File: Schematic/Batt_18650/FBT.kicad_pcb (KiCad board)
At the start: 2 copper layers, 86.5 x 100.5 mm, 18 parts, among them J1 TRRS Connector 3.5, J2 Conn_01x04, SW1 SW_SPDT

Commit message: work on PCBs, logos, and case
did more work on 18650 battery model
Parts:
- removed BT+1: Battery cathode, Connector_PinHeader_2.54mm:PinHeader_1x01_P2.54mm_Vertical
- added ?: , , F.Cu at (92.8, 106.4)
- added BT-2: Battery anode, Connector_PinHeader_2.54mm:PinHeader_1x01_P2.54mm_Vertical, F.Cu at (92.8, 103.9)
- J2: value Conn_01x04 -> TRRS Connector 3.5; footprint Connector_JST:JST_PH_S4B-PH-K_1x04_P2.00mm_Horizontal -> My_Library:PJ-320A
- moved GY2 37.8 mm to (153.8, 143.8)
- moved IMU2 37.5 mm to (153.5, 138.6)
- moved J2 28.9 mm to (140.9, 110.9), turned to 0 degrees
- moved JP1 21.4 mm to (109.1, 68.8)
- moved JP2 12.6 mm to (106.1, 68.8), turned to -90 degrees
- turned IMU1 to -90 degrees
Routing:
- net ESP32_5V5: track 0.00 -> 77.6 mm, vias 0 -> 1
- net GND: track 0.00 -> 42.7 mm
- net Net-(CHGR1-5_VIN): track 0.00 -> 25.3 mm
- net ESP32_3V3: track 18.3 -> 0.00 mm
- net SCL_1: track 3.51 -> 15.3 mm
- net SDA_1: track 9.09 -> 19.5 mm
- net +BATT: track 0.00 -> 7.81 mm
- net Net-(D2-A): track 0.00 -> 7.67 mm
- net Net-(GY2-SCL): track 3.97 -> 0.00 mm
- net Net-(GY2-SDA): track 3.97 -> 0.00 mm
- removed copper zone on B.Cu, net GND
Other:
- board size 86.5 x 100.5 mm -> 86.5 x 77.9 mm

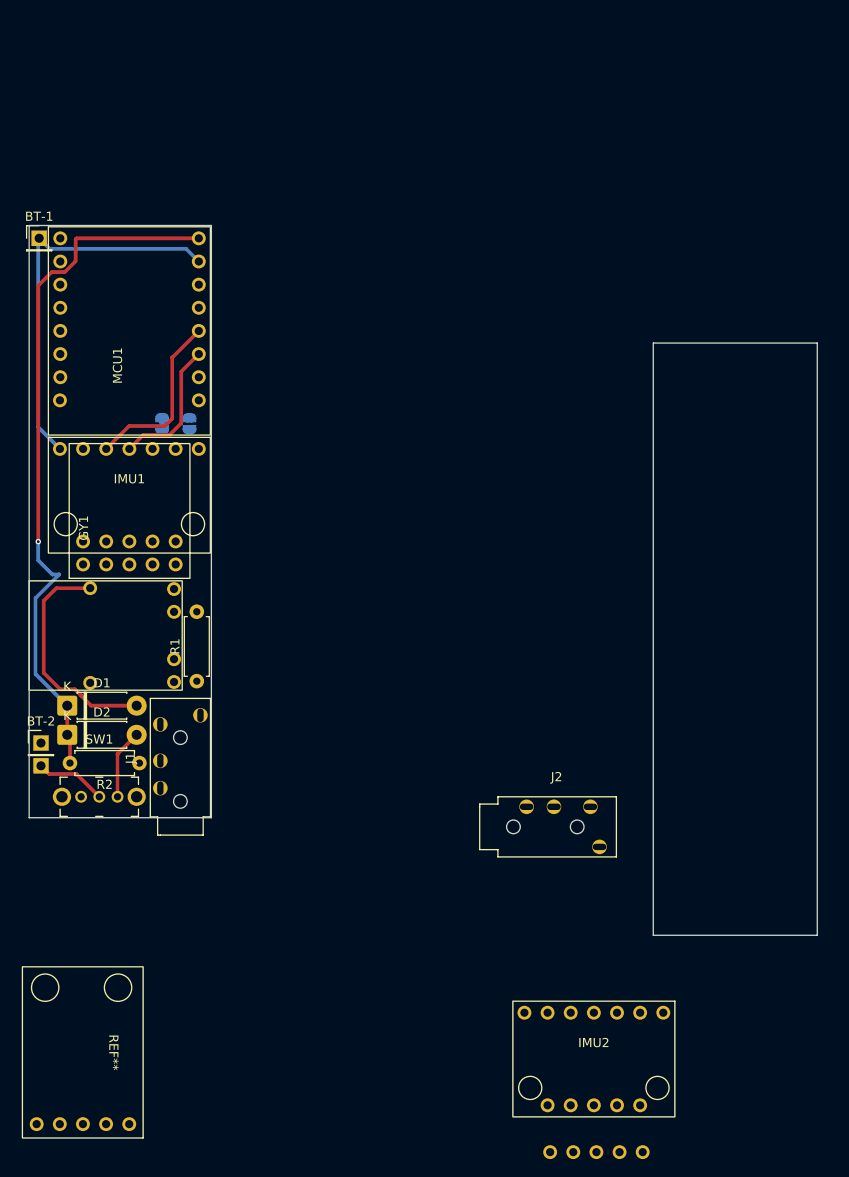
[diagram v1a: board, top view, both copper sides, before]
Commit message: Work on 18650 PCB
It's done, but I may re-do this one to flip the ESP32 sideways...
(I then proceeded to work on the sideways version)
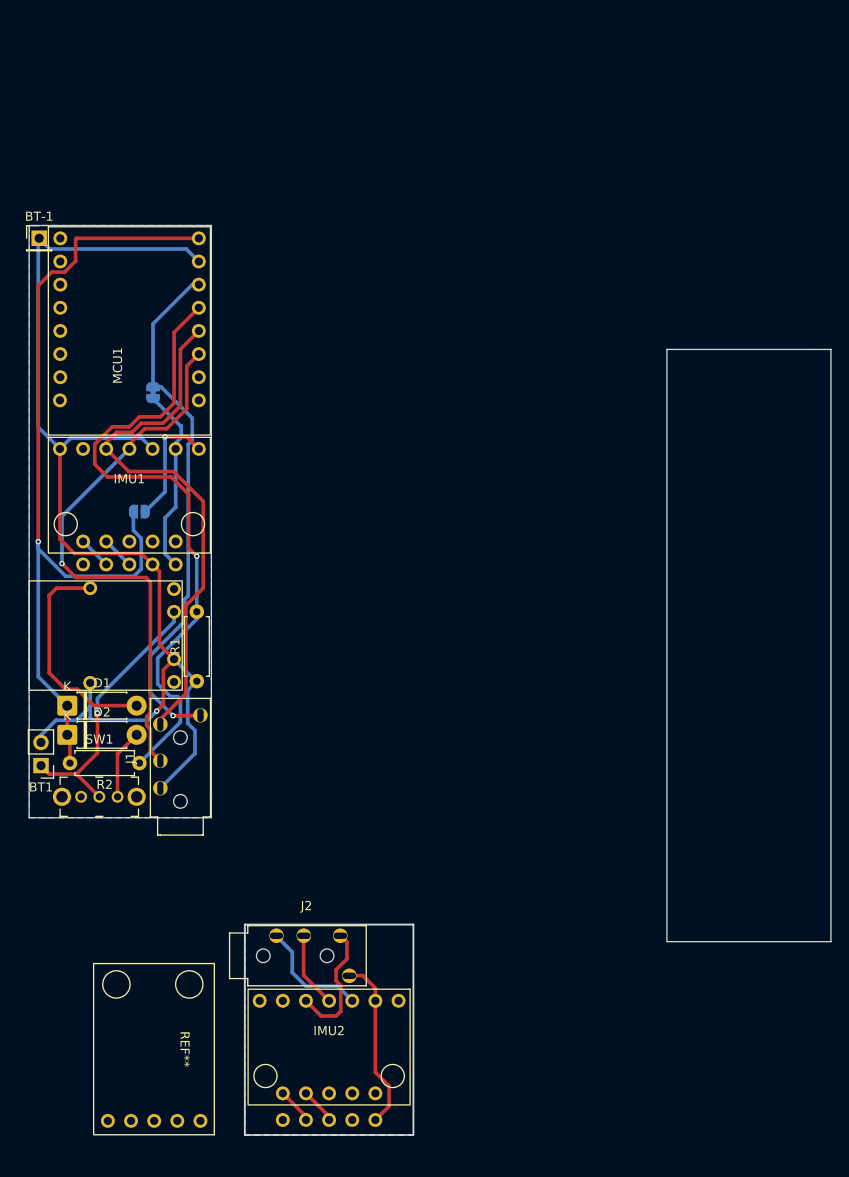
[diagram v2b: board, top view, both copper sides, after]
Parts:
- removed ?: , 
- removed BT-2: Battery anode, Connector_PinHeader_2.54mm:PinHeader_1x01_P2.54mm_Vertical
- added BT1: Battery, Connector_PinHeader_2.54mm:PinHeader_1x02_P2.54mm_Vertical, F.Cu at (92.8, 106.4)
- GY1: moved to B.Cu
- moved J2 30.9 mm to (113.5, 125.0)
- moved GY2 29.6 mm to (124.4, 140.3)
- moved IMU2 29.1 mm to (124.4, 137.3)
- moved JP1 11.1 mm to (103.6, 78.5), turned to 180 degrees
- moved REF** 7.82 mm to (105.1, 137.4)
- moved JP2 3.54 mm to (105.1, 65.5)
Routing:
- net GND: track 42.7 -> 142.3 mm, vias 0 -> 1
- net ESP32_3V3: track 0.00 -> 77.2 mm, vias 0 -> 1
- net BATTERY_READER: track 0.00 -> 71.0 mm, vias 0 -> 1
- net SCL_1: track 15.3 -> 69.8 mm, vias 0 -> 1
- net SDA_1: track 19.5 -> 73.1 mm
- net +BATT: track 7.81 -> 30.0 mm, vias 0 -> 1
- net Net-(GY1-VIN): track 0.00 -> 20.8 mm
- net ESP32_5V5: track 77.6 -> 95.3 mm
- net Net-(IMU1-VIN): track 0.00 -> 13.4 mm, vias 0 -> 1
- net Net-(GY2-SCL): track 0.00 -> 3.97 mm
- net Net-(GY2-SDA): track 0.00 -> 3.97 mm
- net Net-(GY1-SCL): track 0.00 -> 3.58 mm
- net Net-(GY1-SDA): track 0.00 -> 3.58 mm
- net Net-(CHGR1-5_VIN): track 25.3 -> 24.4 mm
- added copper zone on B.Cu, net GND
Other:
- board size 86.5 x 77.9 mm -> 88 x 99.8 mm
- board text added: "Type B Rev. 1.0"
- board text added: "Type C Rev. 1.0"
- board text added: "www.github.com"

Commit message: Final touches for fabrication
Sent designs off to JLBPCB... hopefully they work...
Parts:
- removed BT-1: Battery anode, Connector_PinHeader_2.54mm:PinHeader_1x01_P2.54mm_Vertical
- added BT-2: Battery anode, Connector_PinHeader_2.54mm:PinHeader_1x01_P2.54mm_Vertical, F.Cu at (92.6, 48.5)
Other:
- board text added: "+"
- board text added: "CHGR1"
- board text added: "JLCJLCJLCJLC"
- board text added: "github.com/DrGlaucous/UFBTM"
- board text removed: "www.github.com"

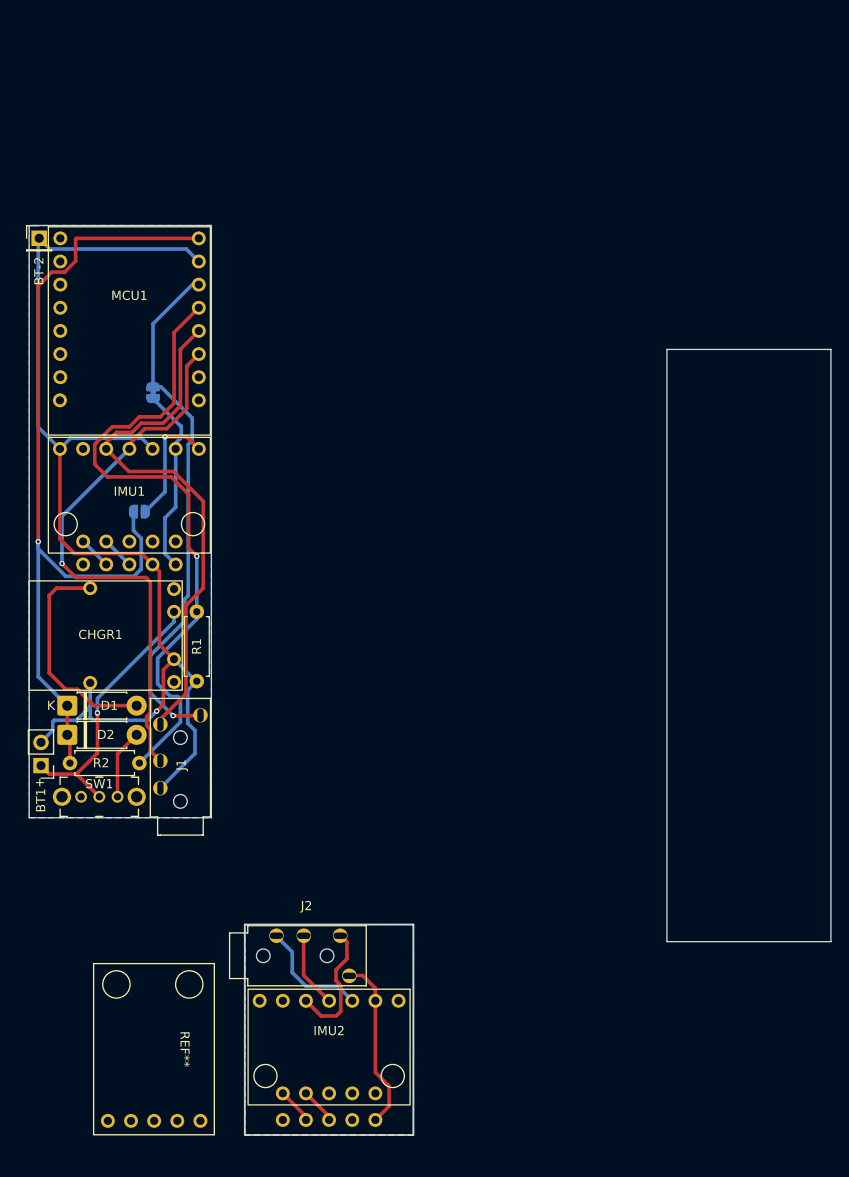
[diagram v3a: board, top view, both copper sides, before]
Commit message: work on correcting Ms. Tracker
it has to be a little bit bigger unfortunately...
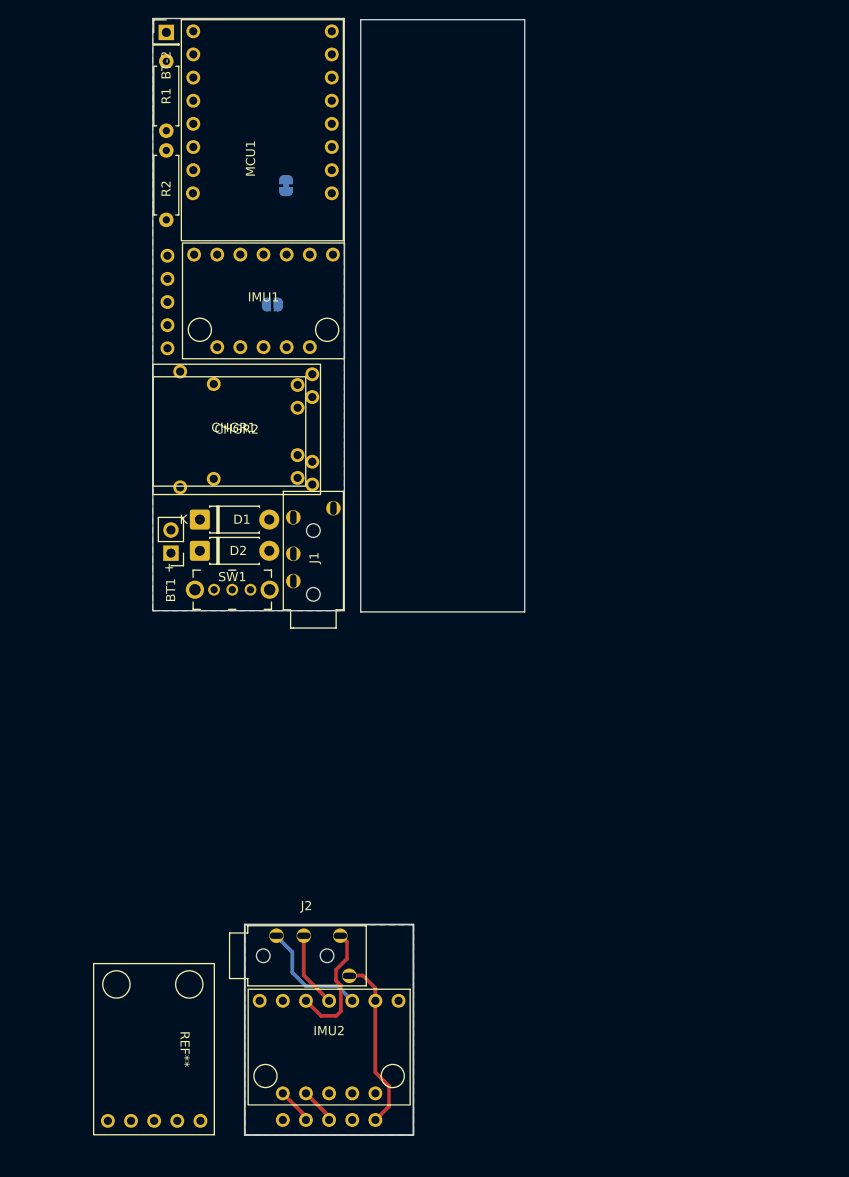
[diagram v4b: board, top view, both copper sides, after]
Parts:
- added CHGR2: ~, My_Library:LX-LBES-Big, F.Cu at (123.5, 62.3)
- MCU1: footprint Espressif:ESP32-C3-SuperMini_PLUS -> Espressif:ESP32-C3-Mini-V1
- moved R1 68.1 mm to (106.6, 29.1), turned to -90 degrees
- moved R2 67.3 mm to (106.6, 38.9), turned to -90 degrees
- moved BT1 27.3 mm to (107.1, 83.1)
- moved JP1 27.0 mm to (118.2, 55.8)
- moved JP2 27.0 mm to (119.7, 42.7)
- moved MCU1 27.0 mm to (117.1, 35.9)
- moved J1 27.0 mm to (120.5, 91.3)
- moved SW1 27.0 mm to (113.8, 87.1)
- moved BT-2 26.6 mm to (106.6, 25.9)
- moved CHGR1 26.2 mm to (121.9, 63.7)
- moved IMU1 25.9 mm to (117.2, 55.4)
- moved GY1 25.5 mm to (111.7, 55.5), turned to 0 degrees
- moved D1 25.1 mm to (110.2, 79.4)
- moved D2 24.9 mm to (110.2, 82.8)
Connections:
- net Net-(CHGR1-5_VIN) renamed /5_VIN_LX
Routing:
- net GND: track 142.4 -> 12.6 mm, vias 1 -> 0
- net ESP32_5V5: track 95.3 -> 0.00 mm, vias 1 -> 0
- net BATTERY_READER: track 71.0 -> 0.00 mm, vias 1 -> 0
- net SCL_1: track 69.8 -> 8.26 mm, vias 1 -> 0
- net SDA_1: track 73.1 -> 14.1 mm
- net ESP32_3V3: track 77.2 -> 19.1 mm, vias 1 -> 0
- net +BATT: track 30.0 -> 0.00 mm, vias 1 -> 0
- net /5_VIN_LX: track 24.4 -> 0.00 mm
- net Net-(GY1-VIN): track 20.8 -> 0.00 mm
- net Net-(IMU1-VIN): track 13.4 -> 0.00 mm, vias 1 -> 0
- net Net-(D2-A): track 7.67 -> 0.00 mm
- net Net-(GY1-SCL): track 3.58 -> 0.00 mm
- net Net-(GY1-SDA): track 3.58 -> 0.00 mm
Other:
- board size 88 x 99.8 mm -> 40.8 x 122.5 mm
